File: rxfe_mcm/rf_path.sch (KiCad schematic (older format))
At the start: 93 parts, among them J401 RF_SHIELD_TWO_PIECES, U401 TRF37B73, U402 MASW-007935-TR3000, U403 MASW-007935-TR3000, U404 TRF37B73, U405 SCLF-25, U406 SMP1330-005LF, U407 SMP1330-005LF, U408 MASW-007935-TR3000, U409 TRF37B73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

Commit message: added some notes/errata to the transmitter schematics
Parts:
- JP401, JP402, JP403, JP504: PN (none) -> 609-3500-ND
- L401, L402, L406, L407: value 18 uH -> 22 uH; PN (none) -> 535-12792-1-ND
- L404: PN (none) -> PM1210-1R2J-RC
- L405, L503: PN (none) -> NLV32T-3R9J-EFD
- U401, U404, U409, U515: footprint Housings_DFN_QFN:DFN-8-1EP_2x2mm_Pitch0.5mm -> footprints:dfn8_s-pwson-n8; PN (none) -> 296-38825-1-ND
- U413: PN (none) -> 1046-1098-1-ND
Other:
- note added: "MASW-007935-TR3000\nV1 LOW, V2 HIGH -- RFC to RF1 \nV1 HIGH, V2 LOW -- RFC to RF2"
- note removed: "MASW-007935-TR3000\nV1 LOW, V2 HIGH -- RFC to V1 \nV1 HIGH, V2 LOW -- RFC to V2"

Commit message: added tvs diodes to external connections on mcm_rxfe
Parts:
- removed JP401, JP402, JP403, JP504: JUMPER, Pin_Headers:Pin_Header_Straight_1x02, symbol JUMPER
- added C546: 22 nF, Capacitors_SMD:C_0603, symbol C_Small
- added D401, D402: LED, LEDs:LED_0603, symbol LED
- added R410, R411, R412, R515: JMP, Resistors_SMD:R_0603, symbol R_Small
- added R413, R414: 10k, Resistors_SMD:R_0603, symbol R_Small
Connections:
- net labels added: TX_OUT
- wire segments 302 -> 310

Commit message: add input protection to mcm usrp front end, modified to also work at kodiak
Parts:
- added JP501: JUMPER3, Pin_Headers:Pin_Header_Straight_1x03, symbol JUMPER3
- added R516, R517: JMP, Resistors_SMD:R_0603, symbol R_Small
- added U516, U517: SMP1330-005LF, TO_SOT_Packages_SMD:SOT-23, symbol SMP1330-005LF
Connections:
- net labels added: CPL_IN
- wire segments 310 -> 319
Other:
- note added: "DNP for KOD"
- note added: "DNP for MCM"
- note added: "DNP for kodiak"
- note added: "RF PATH"
- note added: "first amplifier"
- note added: "for kodiak, set jumper to CPL_IN\nfor mcmurdo, set jumper to USRP_TX"
- note added: "high pass filter"
- note added: "second amplifier"
- note added: "third amplifier"
- note added: "tx amplifier"
- note added: "variable attenuator"
- note removed: "low pass filter"
- moved on the sheet: C553, R504, R505, R506

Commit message: a bit of work on layout..
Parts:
- D401, D402: symbol LED -> LED-RESCUE-rxfe_mcm

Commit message: removed tx path amp, erc fixes
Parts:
- removed C454, C455: 100 nF, Capacitors_SMD:C_0603, symbol C_Small
- removed C456: 10 uF, Capacitors_SMD:C_0603, symbol C_Small
- removed C519: 22 nF, Capacitors_SMD:C_0603, symbol C_Small
- removed L407: 22 uH, Resistors_SMD:R_0805, symbol L_Small
- removed R515: JMP, Resistors_SMD:R_0603, symbol R_Small
- removed U515: TRF37B73, footprints:dfn8_s-pwson-n8, symbol TRF37B73
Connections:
- net PHASING_MATRIX_OUT: now also U407.3 (LIM)
- net at U408.1 (RF1): now also C418.1
- net at C458.2, C546.2: now also C457.1
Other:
- note removed: "tx amplifier"
- moved on the sheet: C426, J401, U407

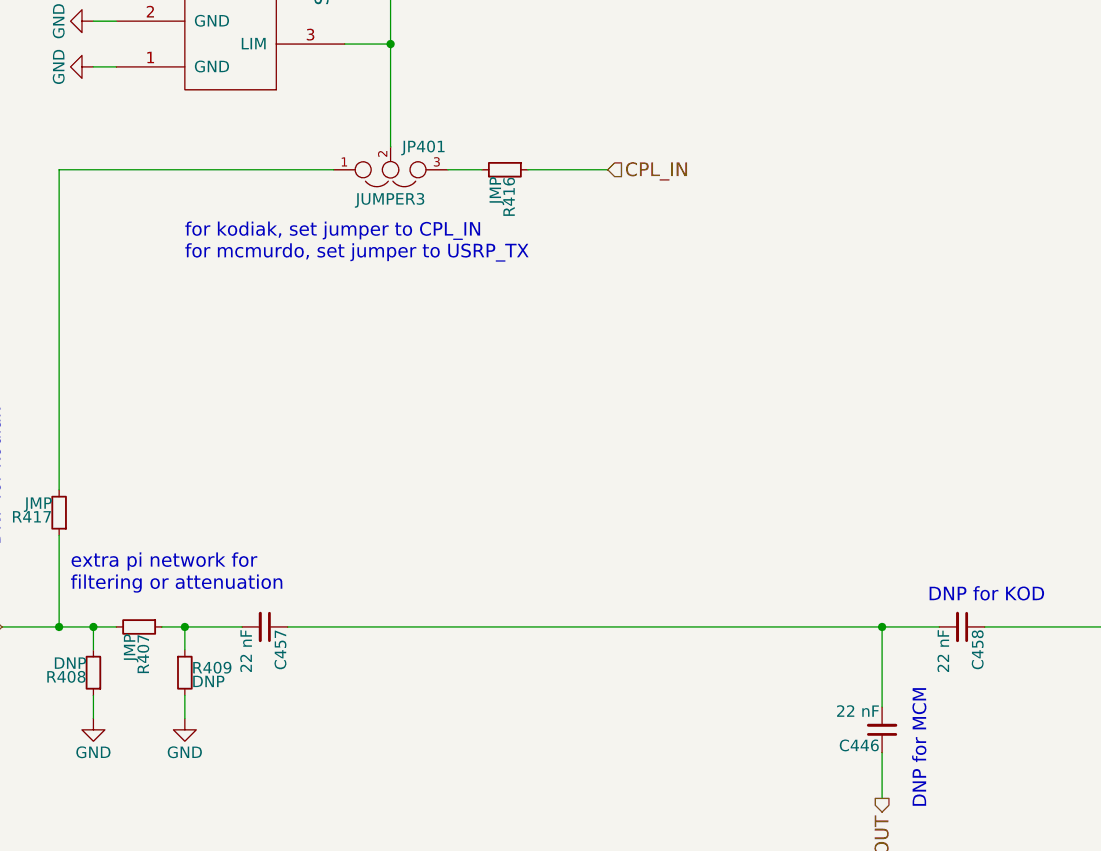
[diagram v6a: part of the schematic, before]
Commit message: finished layout of combined mcm/kod usrp front end board
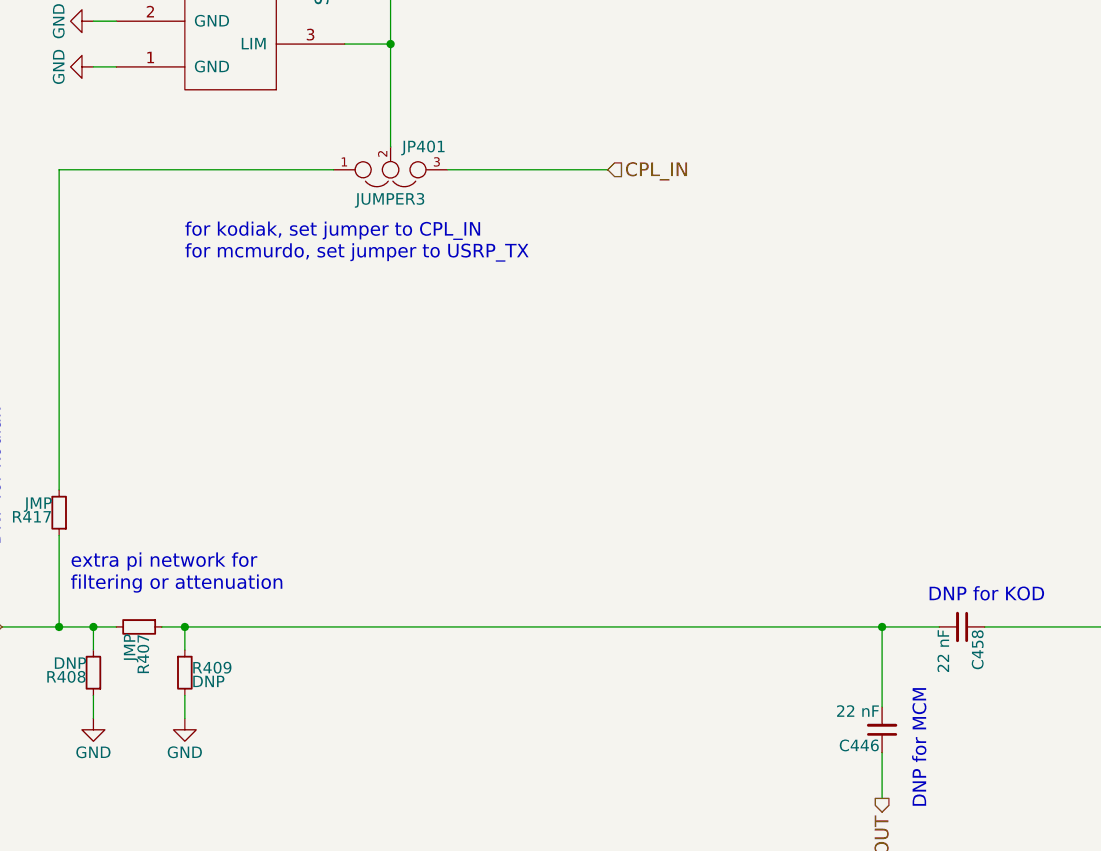
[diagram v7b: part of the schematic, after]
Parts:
- removed C457: 22 nF, Capacitors_SMD:C_0603, symbol C_Small
- removed R516: JMP, Resistors_SMD:R_0603, symbol R_Small
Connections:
- net CPL_IN: now also JP501.3
- net at R407.1, R409.1: now also C458.2, C546.2
